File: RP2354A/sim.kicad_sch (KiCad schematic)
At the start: 11 parts

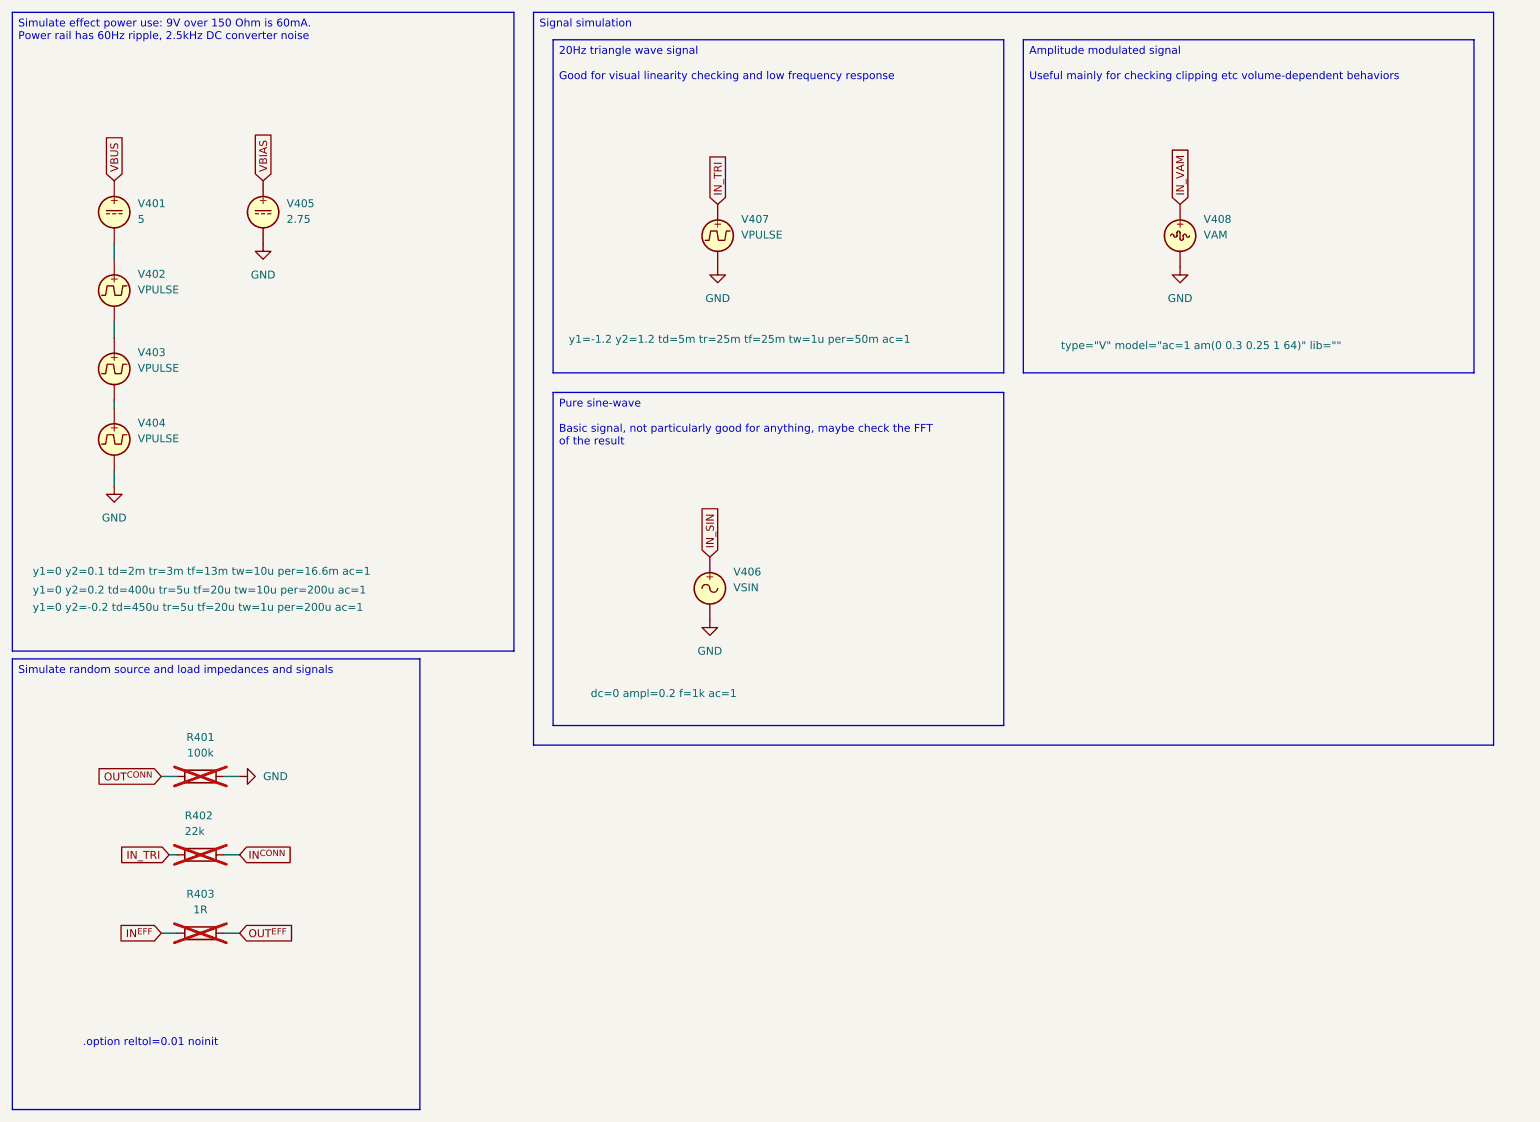
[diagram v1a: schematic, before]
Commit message: rp2354: First stab at pcb layout
This is an insane 6-layer stackup, not because I need six layers
(although it does allow me to be even lazier than usual), but because I
want to use via-in-pad and at that point jlcpcb pretty much ends up
doing the whole precision 6-layer thing anyway.

The minimal RP2354A board makes do with just a simple two-layer stackup,
and I'm sure this could have been done that way too.  But with four
layers it's easy to just use one layer for the +1V1 zone and one for the
+3V3 zone under the RP2354A, and just bring things in with the vias.

This is all connected, but with some ERC noise. Mostly harmless (tm).

Also add JLCPCB part numbers to things, although I need to check them
all several times.

Signed-off-by: Linus Torvalds <torvalds@linux-foundation.org>
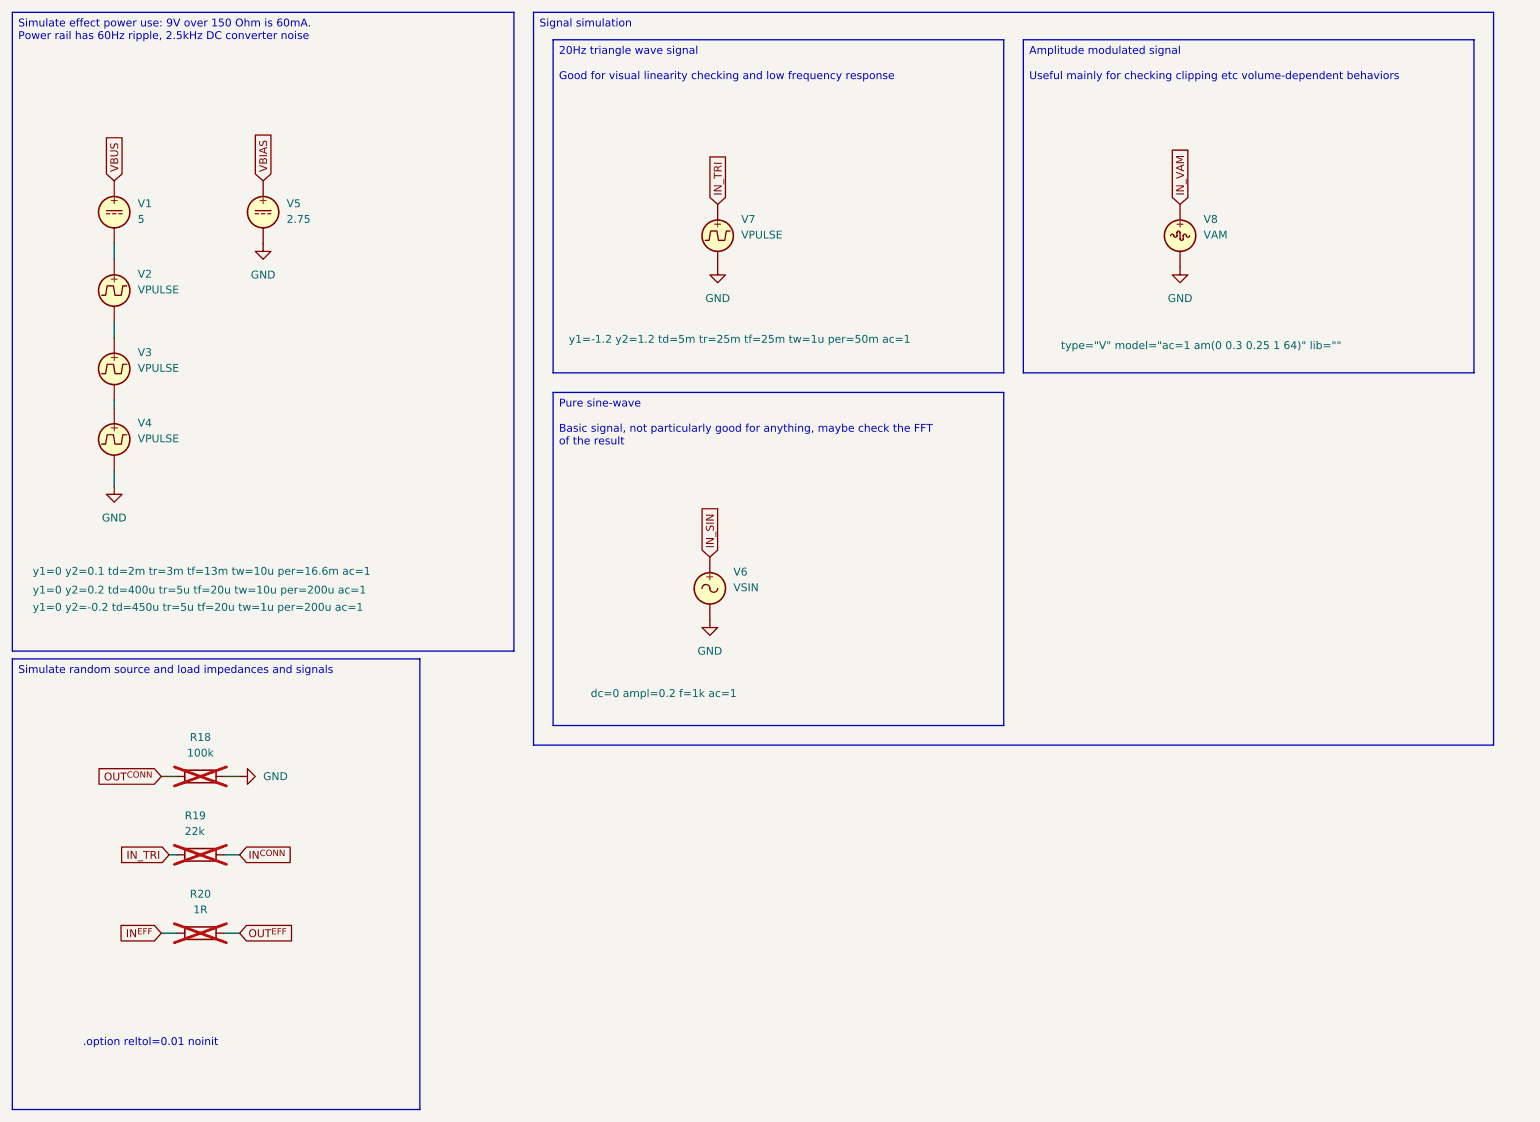
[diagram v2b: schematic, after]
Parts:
- renumbered R401 to R18, R402 to R19, R403 to R20, V401 to V1, V402 to V2, V403 to V3, V404 to V4, V405 to V5, V406 to V6, V407 to V7, V408 to V8
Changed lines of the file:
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@@
 		(on_board no)
 		(dnp no)
-		(property "Reference" "V406"
+		(property "Reference" "V6"
 			(at 130.81 105.2801 0)
 			(effects
@@
 				)
 				(justify left)
+				(hide yes)
+			)
+		)
+		(property "JLCPCB" ""
+			(at 127 107.95 0)
+			(effects
+				(font
+					(size 1.27 1.27)
+				)
 				(hide yes)
 			)
@@
 			(project "Stomp"
 				(path "/9e337e0b-885b-4d2b-99a2-62cdd082c615/a1084b87-85fd-4b63-8fe4-8749c999d338"
-					(reference "V406")
+					(reference "V6")
 					(unit 1)
 				)
@@
 		(on_board no)
 		(dnp no)
-		(property "Reference" "V408"
+		(property "Reference" "V8"
 			(at 207.01 48.1301 0)
 			(effects
@@
 				)
 				(justify left)
+			)
+		)
+		(property "JLCPCB" ""
+			(at 203.2 50.8 0)
+			(effects
+				(font
+					(size 1.27 1.27)
+				)
+				(hide yes)
 			)
 		)
@@
 			(project "Stomp"
 				(path "/9e337e0b-885b-4d2b-99a2-62cdd082c615/a1084b87-85fd-4b63-8fe4-8749c999d338"
-					(reference "V408")
+					(reference "V8")
 					(unit 1)
 				)
@@
 		(dnp yes)
 		(fields_autoplaced yes)
-		(property "Reference" "R401"
+		(property "Reference" "R18"
 			(at 44.45 132.08 90)
 			(effects
@@
 		(property "Description" "Resistor"
 			(at 44.45 138.43 0)
+			(effects
+				(font
+					(size 1.27 1.27)
+				)
+				(hide yes)
+			)
+		)
+		(property "JLCPCB" ""
+			(at 44.45 138.43 90)
 			(effects
 				(font
@@
 			(project "Stomp"
 				(path "/9e337e0b-885b-4d2b-99a2-62cdd082c615/a1084b87-85fd-4b63-8fe4-8749c999d338"
-					(reference "R401")
+					(reference "R18")
 					(unit 1)
 				)
@@
 		(dnp no)
 		(fields_autoplaced yes)
-		(property "Reference" "V405"
+		(property "Reference" "V5"
 			(at 58.42 45.5901 0)
 			(effects
@@
 				)
 				(justify left)
+				(hide yes)
+			)
+		)
+		(property "JLCPCB" ""
+			(at 54.61 46.99 0)
+			(effects
+				(font
+					(size 1.27 1.27)
+				)
 				(hide yes)
 			)
@@
 			(project "RP2354A"
 				(path "/9e337e0b-885b-4d2b-99a2-62cdd082c615/a1084b87-85fd-4b63-8fe4-8749c999d338"
-					(reference "V405")
+					(reference "V5")
 					(unit 1)
 				)
@@
 		(on_board no)
 		(dnp no)
-		(property "Reference" "V402"
+		(property "Reference" "V2"
 			(at 34.29 57.0201 0)
 			(effects
@@
 				)
 				(justify left)
+			)
+		)
+		(property "JLCPCB" ""
+			(at 30.48 59.69 0)
+			(effects
+				(font
+					(size 1.27 1.27)
+				)
+				(hide yes)
 			)
 		)
@@
 			(project "Stomp"
 				(path "/9e337e0b-885b-4d2b-99a2-62cdd082c615/a1084b87-85fd-4b63-8fe4-8749c999d338"
-					(reference "V402")
+					(reference "V2")
 					(unit 1)
 				)
@@
 		(on_board no)
 		(dnp yes)
-		(property "Reference" "R402"
+		(property "Reference" "R19"
 			(at 41.91 144.7799 90)
 			(effects
@@
 		(property "VENDOR" ""
 			(at 44.45 151.13 0)
+			(effects
+				(font
+					(size 1.27 1.27)
+				)
+				(hide yes)
+			)
+		)
+		(property "JLCPCB" ""
+			(at 44.45 151.13 90)
 			(effects
 				(font
@@
 			(project "Stomp"
 				(path "/9e337e0b-885b-4d2b-99a2-62cdd082c615/a1084b87-85fd-4b63-8fe4-8749c999d338"
-					(reference "R402")
+					(reference "R19")
 					(unit 1)
 				)
@@
 		(on_board no)
 		(dnp no)
-		(property "Reference" "V407"
+		(property "Reference" "V7"
 			(at 132.08 48.1301 0)
 			(effects
@@
 				)
 				(justify left)
+			)
+		)
+		(property "JLCPCB" ""
+			(at 128.27 50.8 0)
+			(effects
+				(font
+					(size 1.27 1.27)
+				)
+				(hide yes)
 			)
 		)
@@
 			(project "Stomp"
 				(path "/9e337e0b-885b-4d2b-99a2-62cdd082c615/a1084b87-85fd-4b63-8fe4-8749c999d338"
-					(reference "V407")
+					(reference "V7")
 					(unit 1)
 				)
@@
 		(dnp no)
 		(fields_autoplaced yes)
-		(property "Reference" "V401"
+		(property "Reference" "V1"
 			(at 34.29 45.5901 0)
 			(effects
@@
 				)
 				(justify left)
+				(hide yes)
+			)
+		)
+		(property "JLCPCB" ""
+			(at 30.48 46.99 0)
+			(effects
+				(font
+					(size 1.27 1.27)
+				)
 				(hide yes)
 			)
@@
 			(project "Stomp"
 				(path "/9e337e0b-885b-4d2b-99a2-62cdd082c615/a1084b87-85fd-4b63-8fe4-8749c999d338"
-					(reference "V401")
+					(reference "V1")
 					(unit 1)
 				)
@@
 		(on_board no)
 		(dnp no)
-		(property "Reference" "V404"
+		(property "Reference" "V4"
 			(at 34.29 81.1501 0)
 			(effects
@@
 				)
 				(justify left)
+			)
+		)
+		(property "JLCPCB" ""
+			(at 30.48 83.82 0)
+			(effects
+				(font
+					(size 1.27 1.27)
+				)
+				(hide yes)
 			)
 		)
@@
 			(project "Stomp"
 				(path "/9e337e0b-885b-4d2b-99a2-62cdd082c615/a1084b87-85fd-4b63-8fe4-8749c999d338"
-					(reference "V404")
+					(reference "V4")
 					(unit 1)
 				)
@@
 		(on_board no)
 		(dnp no)
-		(property "Reference" "V403"
+		(property "Reference" "V3"
 			(at 34.29 69.7201 0)
 			(effects
@@
 				)
 				(justify left)
+			)
+		)
+		(property "JLCPCB" ""
+			(at 30.48 72.39 0)
+			(effects
+				(font
+					(size 1.27 1.27)
+				)
+				(hide yes)
 			)
 		)
@@
 			(project "Stomp"
 				(path "/9e337e0b-885b-4d2b-99a2-62cdd082c615/a1084b87-85fd-4b63-8fe4-8749c999d338"
-					(reference "V403")
+					(reference "V3")
 					(unit 1)
 				)
@@
 		(dnp yes)
 		(fields_autoplaced yes)
-		(property "Reference" "R403"
+		(property "Reference" "R20"
 			(at 44.45 157.48 90)
 			(effects
@@
 		(property "Description" "Resistor"
 			(at 44.45 163.83 0)
+			(effects
+				(font
+					(size 1.27 1.27)
+				)
+				(hide yes)
+			)
+		)
+		(property "JLCPCB" ""
+			(at 44.45 163.83 90)
 			(effects
 				(font
@@
 			(project "Boost"
 				(path "/9e337e0b-885b-4d2b-99a2-62cdd082c615/a1084b87-85fd-4b63-8fe4-8749c999d338"
-					(reference "R403")
+					(reference "R20")
 					(unit 1)
 				)

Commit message: Fix missing JLCPCB number, and replace "DNP" with "not in BOM"
Also cross-verify the JLCPCB numbers.

Signed-off-by: Linus Torvalds <torvalds@linux-foundation.org>
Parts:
- R19: footprint Resistor_SMD:R_0805_2012Metric -> (none)
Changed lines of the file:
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@@
 			)
 		)
-		(property "Footprint" "Resistor_SMD:R_0805_2012Metric"
+		(property "Footprint" ""
 			(at 44.45 149.352 90)
 			(effects
